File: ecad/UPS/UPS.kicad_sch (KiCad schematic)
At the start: 0 parts

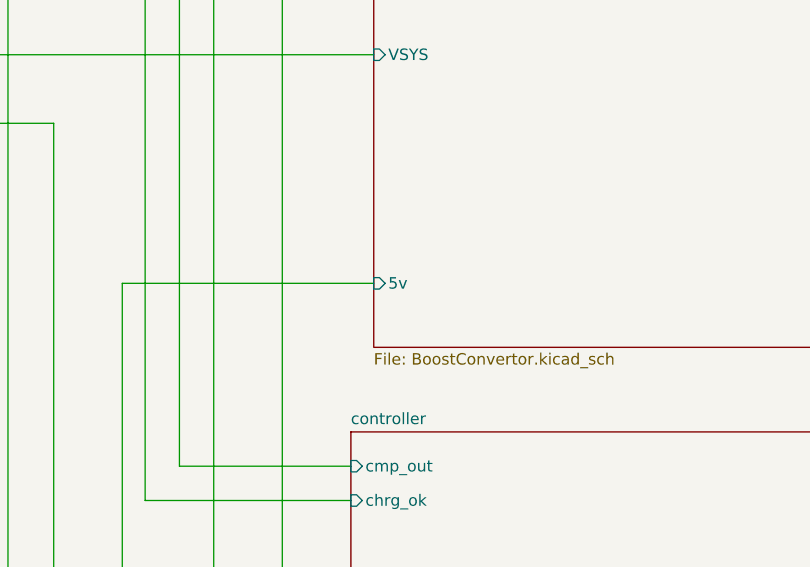
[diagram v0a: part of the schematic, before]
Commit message: Introduce fuses and a bit more routing
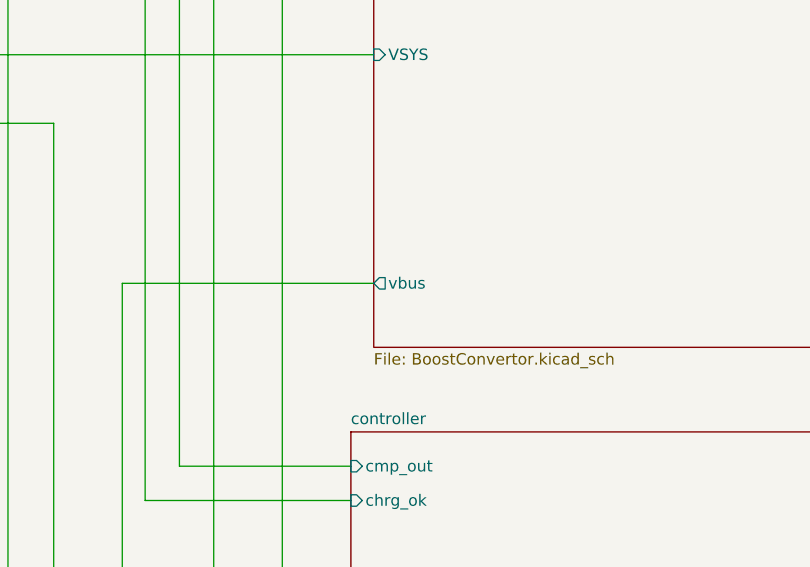
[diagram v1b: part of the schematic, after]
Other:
- sheet BoostConvertor ports: added vbus; removed 5v
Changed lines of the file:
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@@
 			)
 		)
-		(pin "5v" input
+		(pin "vbus" output
 			(at 170.18 80.01 180)
 			(effects

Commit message: More PCB Routing!!!!!
Most of the MCU is done
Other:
- sheet controller ports: added vsel1, vsel2; removed none
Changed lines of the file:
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@@
+	(wire
+		(pts
+			(xy 148.59 143.51) (xy 148.59 124.46)
+		)
+		(stroke
+			(width 0)
+			(type default)
+		)
+	)
+	(wire
+		(pts
+			(xy 149.86 127) (xy 149.86 147.32)
+		)
+		(stroke
+			(width 0)
+			(type default)
+		)
+	)
 	(wire
 		(pts
@@
 	(wire
 		(pts
+			(xy 149.86 147.32) (xy 100.33 147.32)
+		)
+		(stroke
+			(width 0)
+			(type default)
+		)
+	)
+	(wire
+		(pts
 			(xy 121.92 130.81) (xy 121.92 127)
 		)
@@
 	(wire
 		(pts
+			(xy 148.59 124.46) (xy 167.64 124.46)
+		)
+		(stroke
+			(width 0)
+			(type default)
+		)
+	)
+	(wire
+		(pts
 			(xy 100.33 127) (xy 121.92 127)
 		)
@@
 	(wire
 		(pts
+			(xy 100.33 143.51) (xy 148.59 143.51)
+		)
+		(stroke
+			(width 0)
+			(type default)
+		)
+	)
+	(wire
+		(pts
 			(xy 99.06 80.01) (xy 111.76 80.01)
 		)
@@
 		(pts
 			(xy 109.22 85.09) (xy 109.22 153.67)
+		)
+		(stroke
+			(width 0)
+			(type default)
+		)
+	)
+	(wire
+		(pts
+			(xy 167.64 127) (xy 149.86 127)
 		)
 		(stroke
@@
 			(effects
 				(font
+					(size 1.27 1.27)
+				)
+				(justify left)
+			)
+		)
+		(pin "vsel2" output
+			(at 167.64 127 180)
+			(effects
+				(font
+					(size 1.27 1.27)
+				)
+				(justify left)
+			)
+		)
+		(pin "vsel1" output
+			(at 167.64 124.46 180)
+			(effects
+				(font

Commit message: last min pin rearangement
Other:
- sheet controller ports: added vbat_sense; removed none
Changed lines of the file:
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@@
+	(wire
+		(pts
+			(xy 100.33 158.75) (xy 147.32 158.75)
+		)
+		(stroke
+			(width 0)
+			(type default)
+		)
+	)
+	(wire
+		(pts
+			(xy 147.32 158.75) (xy 147.32 110.49)
+		)
+		(stroke
+			(width 0)
+			(type default)
+		)
+	)
 	(wire
 		(pts
@@
 		(pts
 			(xy 149.86 116.84) (xy 149.86 119.38)
+		)
+		(stroke
+			(width 0)
+			(type default)
+		)
+	)
+	(wire
+		(pts
+			(xy 147.32 110.49) (xy 167.64 110.49)
 		)
 		(stroke
@@
 			(effects
 				(font
+					(size 1.27 1.27)
+				)
+				(justify left)
+			)
+		)
+		(pin "vbat_sense" input
+			(at 167.64 110.49 180)
+			(effects
+				(font

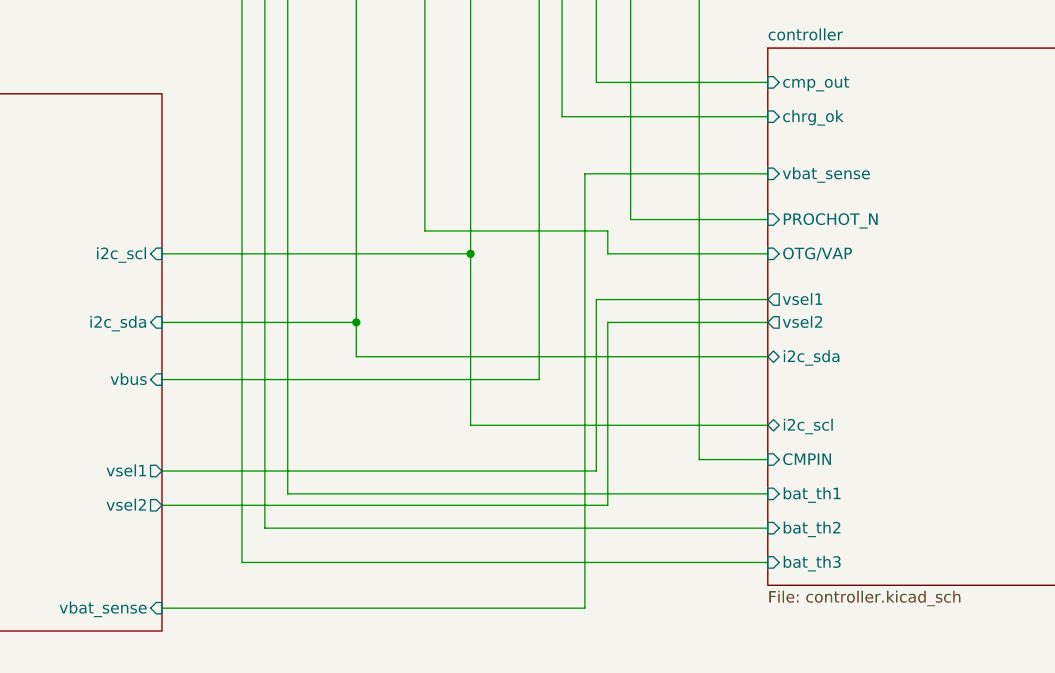
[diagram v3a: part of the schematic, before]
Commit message: VBATSENSE divider put in and some routing
Little more routing, complete by tonight
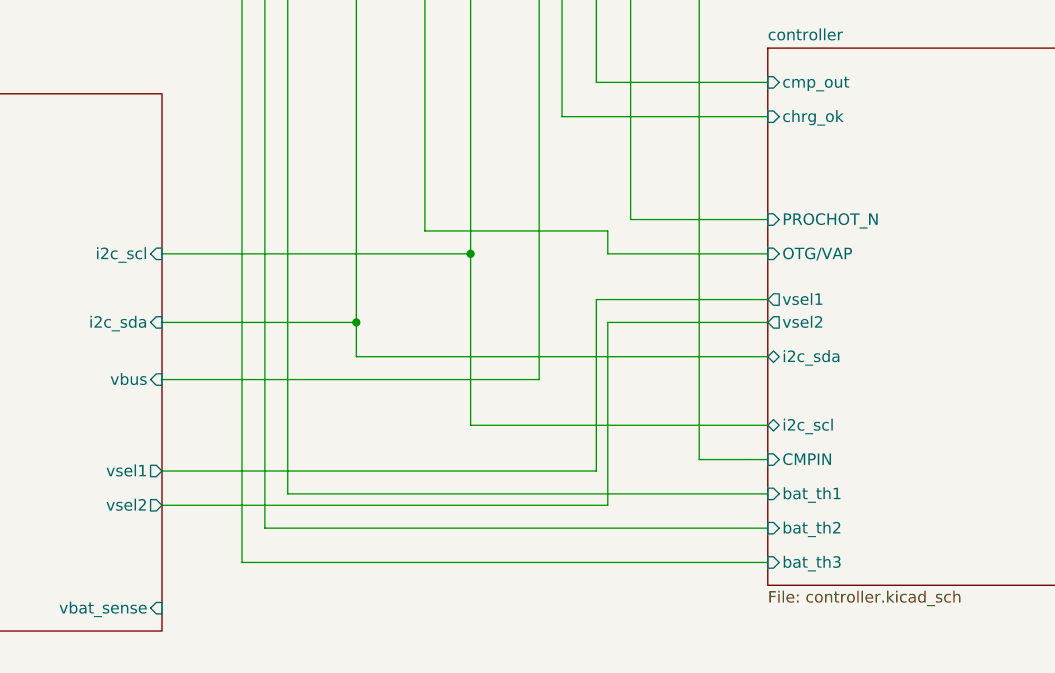
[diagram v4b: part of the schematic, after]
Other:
- sheet controller ports: added none; removed vbat_sense
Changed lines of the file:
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@@
-	(wire
-		(pts
-			(xy 100.33 158.75) (xy 147.32 158.75)
-		)
-		(stroke
-			(width 0)
-			(type default)
-		)
-	)
-	(wire
-		(pts
-			(xy 147.32 158.75) (xy 147.32 110.49)
-		)
-		(stroke
-			(width 0)
-			(type default)
-		)
-	)
 	(wire
 		(pts
@@
 		(pts
 			(xy 149.86 116.84) (xy 149.86 119.38)
-		)
-		(stroke
-			(width 0)
-			(type default)
-		)
-	)
-	(wire
-		(pts
-			(xy 147.32 110.49) (xy 167.64 110.49)
 		)
 		(stroke
@@
 			(effects
 				(font
-					(size 1.27 1.27)
-				)
-				(justify left)
-			)
-		)
-		(pin "vbat_sense" input
-			(at 167.64 110.49 180)
-			(effects
-				(font
